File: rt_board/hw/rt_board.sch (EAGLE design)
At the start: 67 parts, among them IC1 MCP170333MB, IC2/L1 TLE4935L, IC3/L2 TLE4935L, IC4/R1 TLE4935L, IC5/R2 TLE4935L, Q1 8MHz, SW1 B3U-1000PM-B, SW2 B3U-1000PM-B, U1 DRV8801PWP, U2 DRV8801PWP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

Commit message: added 1000uF to +12V input for extra decoupling
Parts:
- added C23: 1000uF, rcl:CPOL-EU153CLV-1014
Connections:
- net +12V: now also C23.+
- net 0V: now also C23.-
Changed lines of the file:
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@@
 <part name="R19" library="rcl" deviceset="R-EU_" device="R0603" value="240R"/>
 <part name="SUPPLY83" library="supply2" deviceset="+5V" device="" value="+3.3V"/>
+<part name="C23" library="rcl" deviceset="CPOL-EU" device="153CLV-1014" value="1000uF"/>
+<part name="SUPPLY87" library="supply2" deviceset="+12V" device=""/>
+<part name="SUPPLY88" library="supply2" deviceset="0V" device=""/>
 </parts>
 <sheets>
@@
 <instance part="R19" gate="G$1" x="38.1" y="101.6" rot="R270"/>
 <instance part="SUPPLY83" gate="+5V" x="38.1" y="111.76"/>
+<instance part="C23" gate="G$1" x="-106.68" y="147.32"/>
+<instance part="SUPPLY87" gate="+12V" x="-106.68" y="154.94"/>
+<instance part="SUPPLY88" gate="0V" x="-106.68" y="137.16"/>
 </instances>
 <busses>
@@
 <wire x1="-86.36" y1="78.74" x2="-83.82" y2="78.74" width="0.1524" layer="91"/>
 </segment>
+<segment>
+<pinref part="C23" gate="G$1" pin="-"/>
+<pinref part="SUPPLY88" gate="0V" pin="0V"/>
+<wire x1="-106.68" y1="139.7" x2="-106.68" y2="142.24" width="0.1524" layer="91"/>
+</segment>
 </net>
 <net name="+5V" class="0">
@@
 <wire x1="-142.24" y1="-198.12" x2="-142.24" y2="-200.66" width="0.1524" layer="91"/>
 </segment>
+<segment>
+<pinref part="C23" gate="G$1" pin="+"/>
+<pinref part="SUPPLY87" gate="+12V" pin="+12V"/>
+<wire x1="-106.68" y1="152.4" x2="-106.68" y2="149.86" width="0.1524" layer="91"/>
+</segment>
 </net>

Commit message: added 4x100nF for Hall sensors
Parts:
- added C24, C25, C26, C27: 100nF, rcl:C-EUC1206
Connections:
- net +5V/1: now also C24.1, C25.1, C26.1, C27.1
- net 0V: now also C24.2, C25.2, C26.2, C27.2
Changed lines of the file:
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@@
 <part name="SUPPLY87" library="supply2" deviceset="+12V" device=""/>
 <part name="SUPPLY88" library="supply2" deviceset="0V" device=""/>
+<part name="C24" library="rcl" deviceset="C-EU" device="C1206" value="100nF"/>
+<part name="C25" library="rcl" deviceset="C-EU" device="C1206" value="100nF"/>
+<part name="C26" library="rcl" deviceset="C-EU" device="C1206" value="100nF"/>
+<part name="C27" library="rcl" deviceset="C-EU" device="C1206" value="100nF"/>
+<part name="SUPPLY89" library="supply2" deviceset="+5V/1" device="" value="+5V"/>
+<part name="SUPPLY90" library="supply2" deviceset="+5V/1" device="" value="+5V"/>
+<part name="SUPPLY91" library="supply2" deviceset="0V" device=""/>
+<part name="SUPPLY92" library="supply2" deviceset="0V" device=""/>
+<part name="SUPPLY93" library="supply2" deviceset="+5V/1" device="" value="+5V"/>
+<part name="SUPPLY94" library="supply2" deviceset="+5V/1" device="" value="+5V"/>
+<part name="SUPPLY95" library="supply2" deviceset="0V" device=""/>
+<part name="SUPPLY96" library="supply2" deviceset="0V" device=""/>
 </parts>
 <sheets>
@@
 <instance part="SUPPLY87" gate="+12V" x="-106.68" y="154.94"/>
 <instance part="SUPPLY88" gate="0V" x="-106.68" y="137.16"/>
+<instance part="C24" gate="G$1" x="-233.68" y="22.86"/>
+<instance part="C25" gate="G$1" x="-233.68" y="2.54"/>
+<instance part="C26" gate="G$1" x="-231.14" y="-137.16"/>
+<instance part="C27" gate="G$1" x="-231.14" y="-157.48"/>
+<instance part="SUPPLY89" gate="G$1" x="-226.06" y="-152.4"/>
+<instance part="SUPPLY90" gate="G$1" x="-226.06" y="-132.08"/>
+<instance part="SUPPLY91" gate="0V" x="-226.06" y="-144.78"/>
+<instance part="SUPPLY92" gate="0V" x="-226.06" y="-165.1"/>
+<instance part="SUPPLY93" gate="G$1" x="-228.6" y="27.94"/>
+<instance part="SUPPLY94" gate="G$1" x="-228.6" y="7.62"/>
+<instance part="SUPPLY95" gate="0V" x="-228.6" y="-5.08"/>
+<instance part="SUPPLY96" gate="0V" x="-228.6" y="15.24"/>
 </instances>
 <busses>
@@
 <pinref part="SUPPLY88" gate="0V" pin="0V"/>
 <wire x1="-106.68" y1="139.7" x2="-106.68" y2="142.24" width="0.1524" layer="91"/>
+</segment>
+<segment>
+<pinref part="C26" gate="G$1" pin="2"/>
+<pinref part="SUPPLY91" gate="0V" pin="0V"/>
+<wire x1="-226.06" y1="-142.24" x2="-231.14" y2="-142.24" width="0.1524" layer="91"/>
+</segment>
+<segment>
+<pinref part="C27" gate="G$1" pin="2"/>
+<pinref part="SUPPLY92" gate="0V" pin="0V"/>
+<wire x1="-226.06" y1="-162.56" x2="-231.14" y2="-162.56" width="0.1524" layer="91"/>
+</segment>
+<segment>
+<pinref part="C25" gate="G$1" pin="2"/>
+<pinref part="SUPPLY95" gate="0V" pin="0V"/>
+<wire x1="-228.6" y1="-2.54" x2="-233.68" y2="-2.54" width="0.1524" layer="91"/>
+</segment>
+<segment>
+<pinref part="C24" gate="G$1" pin="2"/>
+<pinref part="SUPPLY96" gate="0V" pin="0V"/>
+<wire x1="-228.6" y1="17.78" x2="-233.68" y2="17.78" width="0.1524" layer="91"/>
 </segment>
 </net>
@@
 <wire x1="-58.42" y1="149.86" x2="-63.5" y2="149.86" width="0.1524" layer="91"/>
 </segment>
-</net>
+<segment>
+<pinref part="C27" gate="G$1" pin="1"/>
+<pinref part="SUPPLY89" gate="G$1" pin="+5V/1"/>
+<wire x1="-231.14" y1="-154.94" x2="-226.06" y2="-154.94" width="0.1524" layer="91"/>
+</segment>
+<segment>
+<pinref part="C26" gate="G$1" pin="1"/>
+<pinref part="SUPPLY90" gate="G$1" pin="+5V/1"/>
+<wire x1="-231.14" y1="-134.62" x2="-226.06" y2="-134.62" width="0.1524" layer="91"/>
+</segment>
+<segment>
+<pinref part="C24" gate="G$1" pin="1"/>
+<pinref part="SUPPLY93" gate="G$1" pin="+5V/1"/>
+<wire x1="-228.6" y1="25.4" x2="-233.68" y2="25.4" width="0.1524" layer="91"/>
+</segment>
+<segment>
+<pinref part="C25" gate="G$1" pin="1"/>
+<pinref part="SUPPLY94" gate="G$1" pin="+5V/1"/>
+<wire x1="-228.6" y1="5.08" x2="-233.68" y2="5.08" width="0.1524" layer="91"/>
+</segment>
+</net>

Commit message: replaced power connectors with the ones of an aproperiate size
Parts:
- X1, X2, X3: device con-ptr500:AK550/2 -> con-ptr500:AK300/2
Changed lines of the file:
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@@
 <part name="C18" library="rcl" deviceset="CPOL-EU" device="153CLV-0405" value="4.7uF"/>
 <part name="SUPPLY5" library="supply2" deviceset="0V" device=""/>
-<part name="X3" library="con-ptr500" deviceset="AK550/2" device="" value="PWR"/>
+<part name="X3" library="con-ptr500" deviceset="AK300/2" device="" value="PWR"/>
 <part name="F1" library="fuse" deviceset="SH22" device="" value="TF8A"/>
 <part name="SUPPLY6" library="supply2" deviceset="+12V" device=""/>
@@
 <part name="R6" library="rcl" deviceset="R-EU_" device="R0603" value="3kR"/>
 <part name="SUPPLY44" library="supply2" deviceset="0V" device=""/>
-<part name="X1" library="con-ptr500" deviceset="AK550/2" device="" value="LEFT"/>
+<part name="X1" library="con-ptr500" deviceset="AK300/2" device="" value="LEFT"/>
 <part name="U1" library="TI-DRV8801PWP" deviceset="DRV8801PWP" device=""/>
 <part name="SUPPLY45" library="supply2" deviceset="0V" device=""/>
@@
 <part name="R8" library="rcl" deviceset="R-EU_" device="R0603" value="3kR"/>
 <part name="SUPPLY65" library="supply2" deviceset="0V" device=""/>
-<part name="X2" library="con-ptr500" deviceset="AK550/2" device="" value="RIGHT"/>
+<part name="X2" library="con-ptr500" deviceset="AK300/2" device="" value="RIGHT"/>
 <part name="U2" library="TI-DRV8801PWP" deviceset="DRV8801PWP" device=""/>
 <part name="SUPPLY66" library="supply2" deviceset="0V" device=""/>

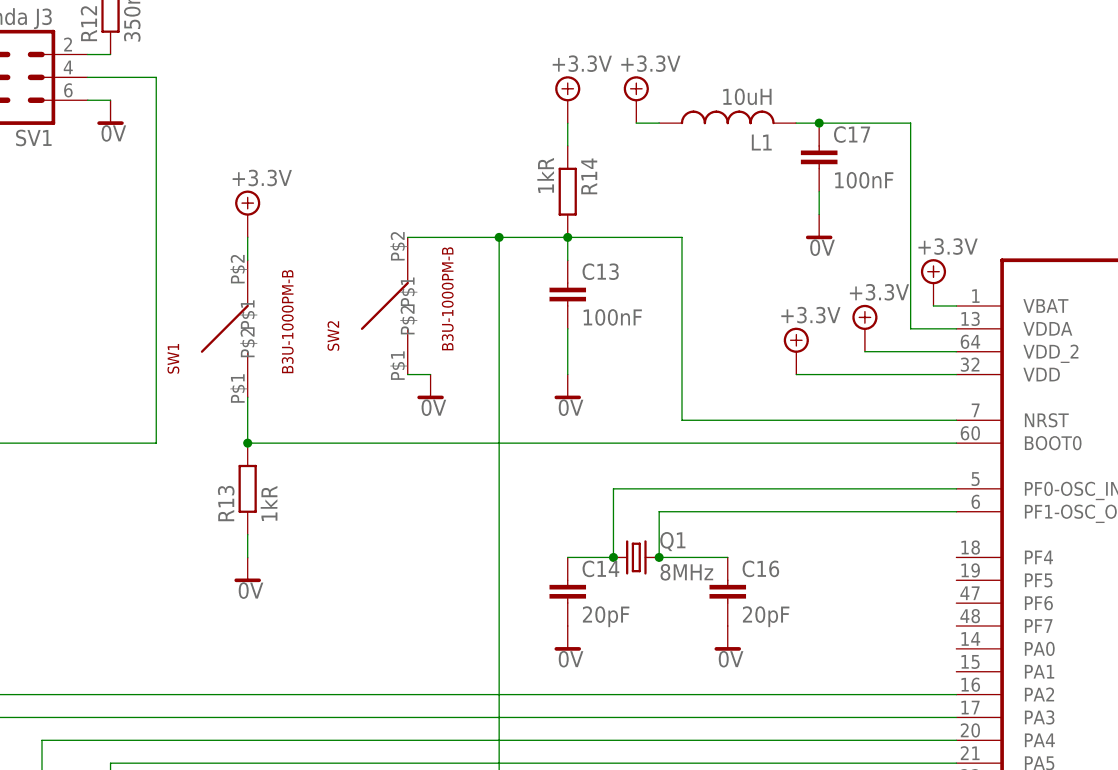
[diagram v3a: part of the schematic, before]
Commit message: removed boot0 button; added 'reest' button decription
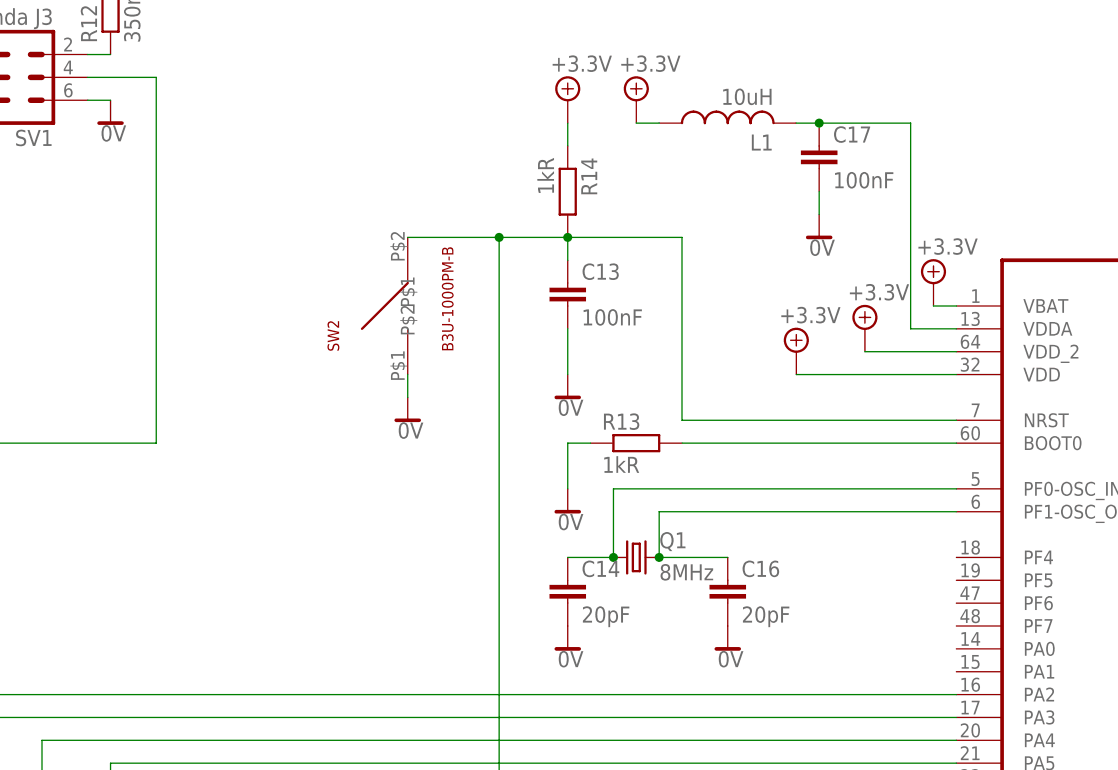
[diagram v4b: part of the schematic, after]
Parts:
- removed SW1: B3U-1000PM-B, basz:B3U-1000PM-B
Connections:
- net +5V: no longer SW1.P$2
- net N$5: no longer SW1.P$1
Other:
- moved on the sheet: R13
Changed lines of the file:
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@@
 <part name="LED2" library="led" deviceset="LED" device="CHIPLED_0603" value="GREEN"/>
 <part name="SUPPLY84" library="supply2" deviceset="+5V" device="" value="+3.3V"/>
-<part name="SW1" library="basz" deviceset="B3U-1000PM-B" device=""/>
 <part name="SW2" library="basz" deviceset="B3U-1000PM-B" device=""/>
-<part name="SUPPLY85" library="supply2" deviceset="+5V" device="" value="+3.3V"/>
 <part name="SUPPLY86" library="supply2" deviceset="0V" device=""/>
 <part name="R18" library="rcl" deviceset="R-EU_" device="R0603" value="240R"/>
@@
 <instance part="SUPPLY8" gate="+5V" x="30.48" y="147.32"/>
 <instance part="SUPPLY9" gate="0V" x="30.48" y="134.62"/>
-<instance part="R13" gate="G$1" x="-104.14" y="66.04" rot="R90"/>
-<instance part="SUPPLY10" gate="0V" x="-104.14" y="55.88"/>
+<instance part="R13" gate="G$1" x="-60.96" y="71.12"/>
+<instance part="SUPPLY10" gate="0V" x="-68.58" y="63.5"/>
 <instance part="R14" gate="G$1" x="-68.58" y="99.06" rot="R270"/>
 <instance part="C13" gate="G$1" x="-68.58" y="88.9"/>
@@
 <instance part="LED2" gate="G$1" x="27.94" y="91.44"/>
 <instance part="SUPPLY84" gate="+5V" x="27.94" y="111.76"/>
-<instance part="SW1" gate="G$1" x="-104.14" y="83.82" rot="R90"/>
 <instance part="SW2" gate="G$1" x="-86.36" y="86.36" rot="R90"/>
-<instance part="SUPPLY85" gate="+5V" x="-104.14" y="96.52"/>
-<instance part="SUPPLY86" gate="0V" x="-83.82" y="76.2"/>
+<instance part="SUPPLY86" gate="0V" x="-86.36" y="73.66"/>
 <instance part="R18" gate="G$1" x="27.94" y="101.6" rot="R270"/>
 <instance part="LED3" gate="G$1" x="38.1" y="91.44"/>
@@
 <pinref part="R13" gate="G$1" pin="1"/>
 <pinref part="SUPPLY10" gate="0V" pin="0V"/>
-<wire x1="-104.14" y1="58.42" x2="-104.14" y2="60.96" width="0.1524" layer="91"/>
+<wire x1="-68.58" y1="66.04" x2="-68.58" y2="71.12" width="0.1524" layer="91"/>
+<wire x1="-68.58" y1="71.12" x2="-66.04" y2="71.12" width="0.1524" layer="91"/>
 </segment>
 <segment>
@@
 <pinref part="SW2" gate="G$1" pin="P$1"/>
 <pinref part="SUPPLY86" gate="0V" pin="0V"/>
-<wire x1="-86.36" y1="78.74" x2="-83.82" y2="78.74" width="0.1524" layer="91"/>
+<wire x1="-86.36" y1="78.74" x2="-86.36" y2="76.2" width="0.1524" layer="91"/>
 </segment>
 <segment>
@@
 </segment>
 <segment>
-<pinref part="SW1" gate="G$1" pin="P$2"/>
-<pinref part="SUPPLY85" gate="+5V" pin="+5V"/>
-<wire x1="-104.14" y1="91.44" x2="-104.14" y2="93.98" width="0.1524" layer="91"/>
-</segment>
-<segment>
 <pinref part="R18" gate="G$1" pin="1"/>
 <pinref part="SUPPLY84" gate="+5V" pin="+5V"/>
@@
 <pinref part="U6" gate="A" pin="BOOT0"/>
 <pinref part="R13" gate="G$1" pin="2"/>
-<wire x1="-104.14" y1="71.12" x2="-25.4" y2="71.12" width="0.1524" layer="91"/>
-<pinref part="SW1" gate="G$1" pin="P$1"/>
-<wire x1="-104.14" y1="76.2" x2="-104.14" y2="71.12" width="0.1524" layer="91"/>
-<junction x="-104.14" y="71.12"/>
+<wire x1="-55.88" y1="71.12" x2="-25.4" y2="71.12" width="0.1524" layer="91"/>
 </segment>
 </net>
